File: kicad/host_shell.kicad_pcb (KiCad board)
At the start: 2 copper layers, 90 x 100 mm, 240 parts, among them J1 FG PH-2AWT, J10 Memory Card Slot, J11 Conn_02x12_Odd_Even, J2 Conn_01x02, J3 Conn_01x02, J4 Conn_01x40, J5 Conn_02x10_Odd_Even, J6 Conn_01x03, J7 Conn_01x02, J8 PJ-316A-6A, J9 Conn_01x02, P1 TYPE-C16PIN, Q1 IRLML2246TRPBF, Q4 BSS138W, Q5 BSS84W, Q6 BSS138W, Q7 BSS138W, SW1 GT-TC018A-H0375-L1, SW10 PTS645SL50SMTR92, SW11 SKRPACE010_6, SW12 PTS645SL50SMTR92, SW13 PTS645SL50SMTR92, SW2 PTS645SL50SMTR92, SW3 PTS645SL50SMTR92, SW4 PTS645SL50SMTR92, SW5 PTS645SL50SMTR92, SW6 PTS645SL50SMTR92, SW7 PTS645SL50SMTR92, SW8 PTS645SL50SMTR92, SW9 PTS645SL50SMTR92, U1 MCP73831-2-OT, U10 LM4880MX/NOPB, U11 LM4890S, U12 SN74LVC1G3157DBVR, U13 SN74AHC541PWR, U14 TPS22919DCKR, U15 RV-3028-C7, U2 XC6194AA03ER-G, U3 TPS63802, U4 PCA9555PW, U5 W25Q32JVSSIQ, U6 APS6404L-3SQRx-SN, U7 RP2350B, U8 74LVC2G17GW, U9 LM4890S, Y1 ABM8-272-T3

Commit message: add silks
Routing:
- net /EXTVIDENX: track 101.9 -> 103.1 mm
- net GND: vias 606 -> 609
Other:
- outline, holes or cut-outs redrawn
- board text added: "A"
- board text added: "B"
- board text added: "HOME"
- board text added: "SELECT"
- board text added: "START"
- board text added: "X"
- board text added: "Y"
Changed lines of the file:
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@@
 		(tags "SPST Button Switch CK C&K")
 		(property "Reference" "SW9"
-			(at 0 4.05 0)
+			(at 0 -4 0)
 			(layer "B.SilkS")
 			(effects
@@
 		(tags "SPST Button Switch CK C&K")
 		(property "Reference" "SW6"
-			(at 0 4.05 0)
+			(at 0 -4 0)
 			(layer "B.SilkS")
 			(effects
@@
 		(tags "SPST Button Switch CK C&K")
 		(property "Reference" "SW12"
-			(at 0 4.05 90)
+			(at -5.5 0 180)
 			(layer "B.SilkS")
 			(effects
@@
 		(tags "SPST Button Switch CK C&K")
 		(property "Reference" "SW13"
-			(at 0 4.05 90)
+			(at -5.5 0 180)
 			(layer "B.SilkS")
 			(effects
@@
 		(tags "SPST Button Switch CK C&K")
 		(property "Reference" "SW8"
-			(at 0 4.05 180)
+			(at 0 -4 180)
 			(layer "B.SilkS")
 			(effects
@@
 		(tags "SPST Button Switch CK C&K")
 		(property "Reference" "SW10"
-			(at 0 4.05 180)
+			(at 0 -4 180)
 			(layer "B.SilkS")
 			(effects
@@
 		(layer "Edge.Cuts")
 	)
+	(gr_circle
+		(center 125 128)
+		(end 126 128)
+		(stroke
+			(width 0.05)
+			(type default)
+		)
+		(fill no)
+		(layer "Edge.Cuts")
+	)
 	(gr_line
 		(start 145 53)
@@
 		)
 	)
+	(gr_text "B"
+		(at 64.7 133 0)
+		(layer "B.SilkS")
+		(effects
+			(font
+				(size 2 2)
+				(thickness 0.3)
+			)
+			(justify mirror)
+		)
+	)
+	(gr_text "Y"
+		(at 75 123 0)
+		(layer "B.SilkS")
+		(effects
+			(font
+				(size 2 2)
+				(thickness 0.3)
+			)
+			(justify mirror)
+		)
+	)
+	(gr_text "A"
+		(at 75 143 0)
+		(layer "B.SilkS")
+		(effects
+			(font
+				(size 2 2)
+				(thickness 0.3)
+			)
+			(justify mirror)
+		)
+	)
+	(gr_text "X"
+		(at 85 133 0)
+		(layer "B.SilkS")
+		(effects
+			(font
+				(size 2 2)
+				(thickness 0.3)
+			)
+			(justify mirror)
+		)
+	)
+	(gr_text "START"
+		(at 90 149.45 0)
+		(layer "B.SilkS")
+		(effects
+			(font
+				(size 2 2)
+				(thickness 0.3)
+			)
+			(justify mirror)
+		)
+	)
+	(gr_text "HOME"
+		(at 100 128 0)
+		(layer "B.SilkS")
+		(effects
+			(font
+				(size 2 2)
+				(thickness 0.3)
+			)
+			(justify mirror)
+		)
+	)
+	(gr_text "SELECT"
+		(at 110.2225 149.5 0)
+		(layer "B.SilkS")
+		(effects
+			(font
+				(size 2 2)
+				(thickness 0.3)
+			)
+			(justify mirror)
+		)
+	)
 	(segment
 		(start 112.5 138.95)
@@
 	)
 	(via
+		(at 123.2 126.7)
+		(size 0.6)
+		(drill 0.3)
+		(layers "F.Cu" "B.Cu")
+		(net "GND")
+	)
+	(via
+		(at 121.8 132.2)
+		(size 0.6)
+		(drill 0.3)
+		(layers "F.Cu" "B.Cu")
+		(net "GND")
+	)
+	(via
 		(at 130.7 106.7)
 		(size 0.6)
@@
 	)
 	(via
-		(at 124.7 121.2)
+		(at 123.8 119.6)
 		(size 0.6)
 		(drill 0.3)
@@
 	)
 	(via
-		(at 121.9 128.4)
+		(at 123.2 122.5)
 		(size 0.6)
 		(drill 0.3)
@@
 	)
 	(via
+		(at 121.8 126.7)
+		(size 0.6)
+		(drill 0.3)
+		(layers "F.Cu" "B.Cu")
+		(net "GND")
+	)
+	(via
 		(at 76.7 64.3)
 		(size 0.6)
@@
 	)
 	(segment
-		(start 75.5 130.4)
-		(end 75.3 130.2)
+		(start 75.5 142.4)
+		(end 75.5 130.4)
 		(width 0.15)
 		(layer "B.Cu")
@@
 	)
 	(segment
-		(start 84.9 145)
-		(end 78.1 145)
+		(start 126.6 118.1)
+		(end 122.5 122.2)
 		(width 0.15)
 		(layer "B.Cu")
@@
 	)
 	(segment
-		(start 136.35 112.54)
-		(end 136.35 115.15)
+		(start 120.7 143.2)
+		(end 86.7 143.2)
 		(width 0.15)
 		(layer "B.Cu")
@@
 	)
 	(segment
-		(start 75.5 142.4)
-		(end 75.5 130.4)
+		(start 133.4 118.1)
+		(end 126.6 118.1)
 		(width 0.15)
 		(layer "B.Cu")
@@
 	)
 	(segment
-		(start 133.4 118.1)
-		(end 126.6 118.1)
+		(start 136.35 112.54)
+		(end 136.35 115.15)
 		(width 0.15)
 		(layer "B.Cu")
@@
 	)
 	(segment
-		(start 126.6 118.1)
-		(end 123.9 120.8)
+		(start 123.9 140)
+		(end 120.7 143.2)
 		(width 0.15)
 		(layer "B.Cu")
@@
 	)
 	(segment
-		(start 120.7 143.2)
-		(end 86.7 143.2)
+		(start 86.7 143.2)
+		(end 84.9 145)
 		(width 0.15)
 		(layer "B.Cu")
@@
 	)
 	(segment
-		(start 123.9 140)
-		(end 120.7 143.2)
+		(start 75.5 130.4)
+		(end 75.3 130.2)
 		(width 0.15)
 		(layer "B.Cu")
@@
 	)
 	(segment
-		(start 86.7 143.2)
-		(end 84.9 145)
+		(start 136.35 115.15)
+		(end 133.4 118.1)
 		(width 0.15)
 		(layer "B.Cu")
@@
 	)
 	(segment
-		(start 136.35 115.15)
-		(end 133.4 118.1)
+		(start 123.9 134.5)
+		(end 123.9 140)
 		(width 0.15)
 		(layer "B.Cu")
@@
 	)
 	(segment
-		(start 123.9 120.8)
-		(end 123.9 140)
+		(start 84.9 145)
+		(end 78.1 145)
+		(width 0.15)
+		(layer "B.Cu")
+		(net "/EXTVIDENX")
+	)
+	(segment
+		(start 122.5 133.1)
+		(end 123.9 134.5)
+		(width 0.15)
+		(layer "B.Cu")
+		(net "/EXTVIDENX")
+	)
+	(segment
+		(start 122.5 122.2)
+		(end 122.5 133.1)
 		(width 0.15)
 		(layer "B.Cu")
@@
 			"9daddf93-e06c-4a59-9522-627f97df5188" "9e0cef42-f97c-4f43-843b-7f8c4ffe4ac2"
 			"abaa75ca-23c1-4a3f-aca2-469630cf8e8c" "ba1a4a74-69e7-4510-a430-9c96d14ca659"
-			"d73ac5a4-f9f1-4aa2-99ab-cd256f9330ab" "f0571547-1e29-4fb5-9b20-fcf055b88a4c"
+			"bb25cce4-5bdf-4cbd-8a70-fee24dea32b7" "d73ac5a4-f9f1-4aa2-99ab-cd256f9330ab"
+			"f0571547-1e29-4fb5-9b20-fcf055b88a4c"
 		)
 	)

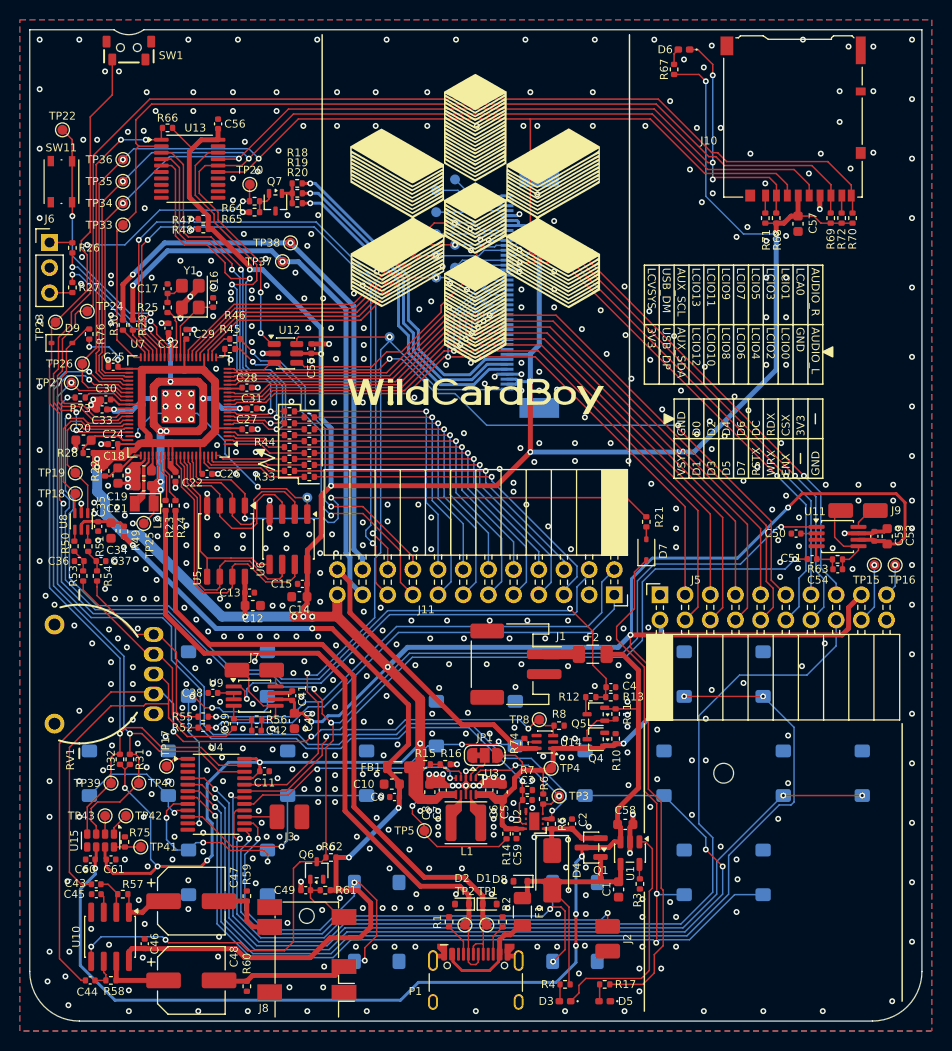
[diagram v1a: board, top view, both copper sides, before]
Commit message: fix L/R of speaker and bumper
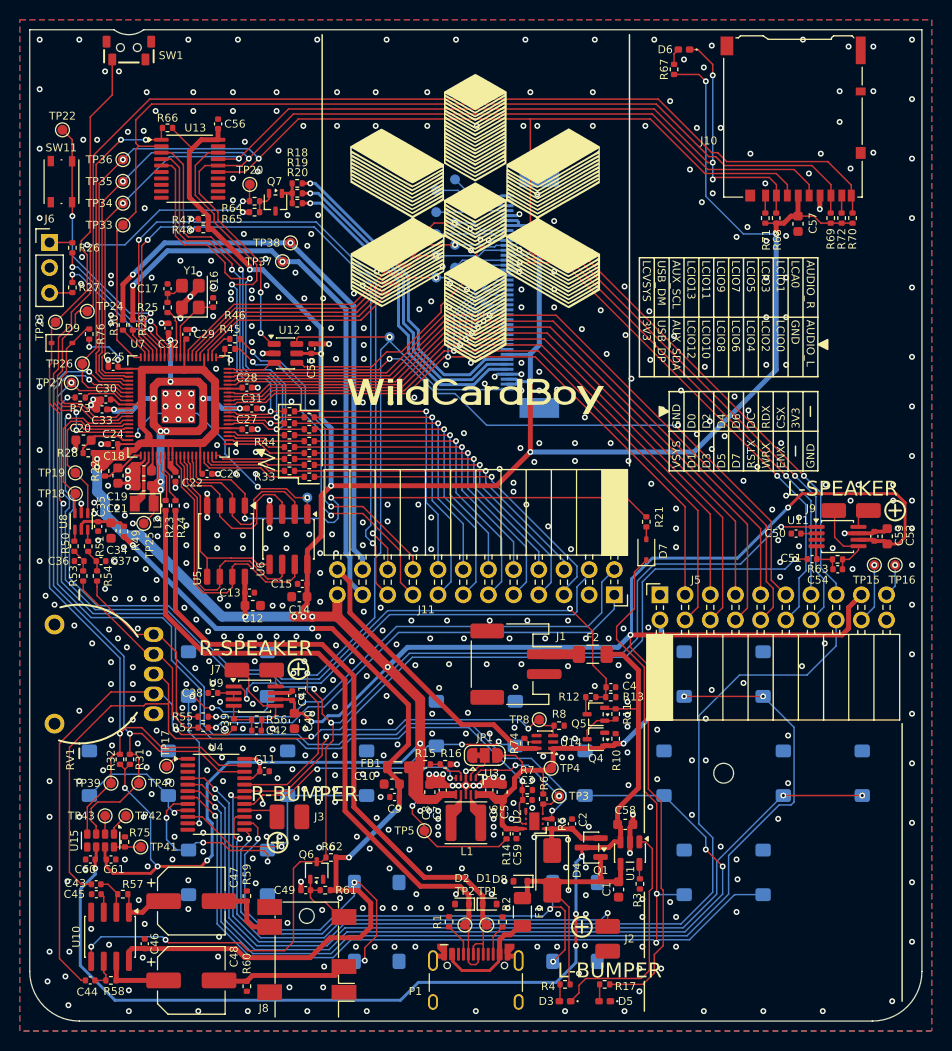
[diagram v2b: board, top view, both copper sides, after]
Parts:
- added G***: LOGO, LOGO, B.Cu at (100.0, 114.0)
- moved J9 0.70 mm to (137.8, 101.5)
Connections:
- net Net-(J7-Pin_1) renamed /SPK_R+
- net Net-(J7-Pin_2) renamed /SPK_R-
- net Net-(J9-Pin_1) renamed /SPK_L+
- net Net-(J9-Pin_2) renamed /SPK_L-
- net Net-(U4-IO0_0) renamed /BTN_L
- net Net-(U4-IO0_1) renamed /BTN_R
- net Net-(U4-IO0_2) renamed /BTN_U
- net Net-(U4-IO0_4) renamed /BTN_A
- net Net-(U4-IO0_5) renamed /BTN_B
- net Net-(U4-IO0_6) renamed /BTN_X
- net Net-(U4-IO0_7) renamed /BTN_Y
- net Net-(U4-IO1_0) renamed /BTN_SEL
- net Net-(U4-IO1_1) renamed /BTN_STA
- net Net-(U4-IO1_4) renamed /BTN_HOME
- C43 pad 2: Net-(C39-Pad2) -> Net-(C43-Pad2)
- C44 pad 2: Net-(C44-Pad2) -> Net-(C39-Pad2)
- C51 pad 2: Net-(C44-Pad2) -> Net-(C43-Pad2)
- J2 pad 1: Net-(J2-Pin_1) -> /BTN_BL
- J3 pad 1: Net-(J3-Pin_1) -> /BTN_BR
- RV1 pad 2A: Net-(C39-Pad2) -> Net-(C43-Pad2)
- RV1 pad 2B: Net-(C44-Pad2) -> Net-(C39-Pad2)
- U4 pad 15: Net-(J3-Pin_1) -> /BTN_BL
- U4 pad 16: Net-(J2-Pin_1) -> /BTN_BR
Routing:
- net Net-(C44-Pad2): track 117.6 -> 0.00 mm, vias 3 -> 0
- net Net-(C43-Pad2): track 0.00 -> 109.5 mm, vias 0 -> 2
- net Net-(J2-Pin_1): track 52.8 -> 0.00 mm, vias 2 -> 0
- net /BTN_BL: track 0.00 -> 52.1 mm, vias 0 -> 2
- net Net-(C39-Pad2): track 40.2 -> 48.3 mm, vias 0 -> 1
- net /BTN_BR: track 0.00 -> 3.56 mm
- net Net-(J3-Pin_1): track 3.29 -> 0.00 mm
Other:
- board text added: "L-BUMPER"
- board text added: "L-SPEAKER"
- board text added: "R-BUMPER"
- board text added: "R-SPEAKER"
